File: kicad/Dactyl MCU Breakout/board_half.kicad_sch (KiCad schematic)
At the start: 30 parts, among them J301 JST, J302 Split, J303 Column, J304 Thumb, J305 External, J306 Row, J307 Display, J308 Vic, SW301 Battery, SW302 Reset, SW303 LED, U301 SRV05-4, U302 Nice!Nano/2040

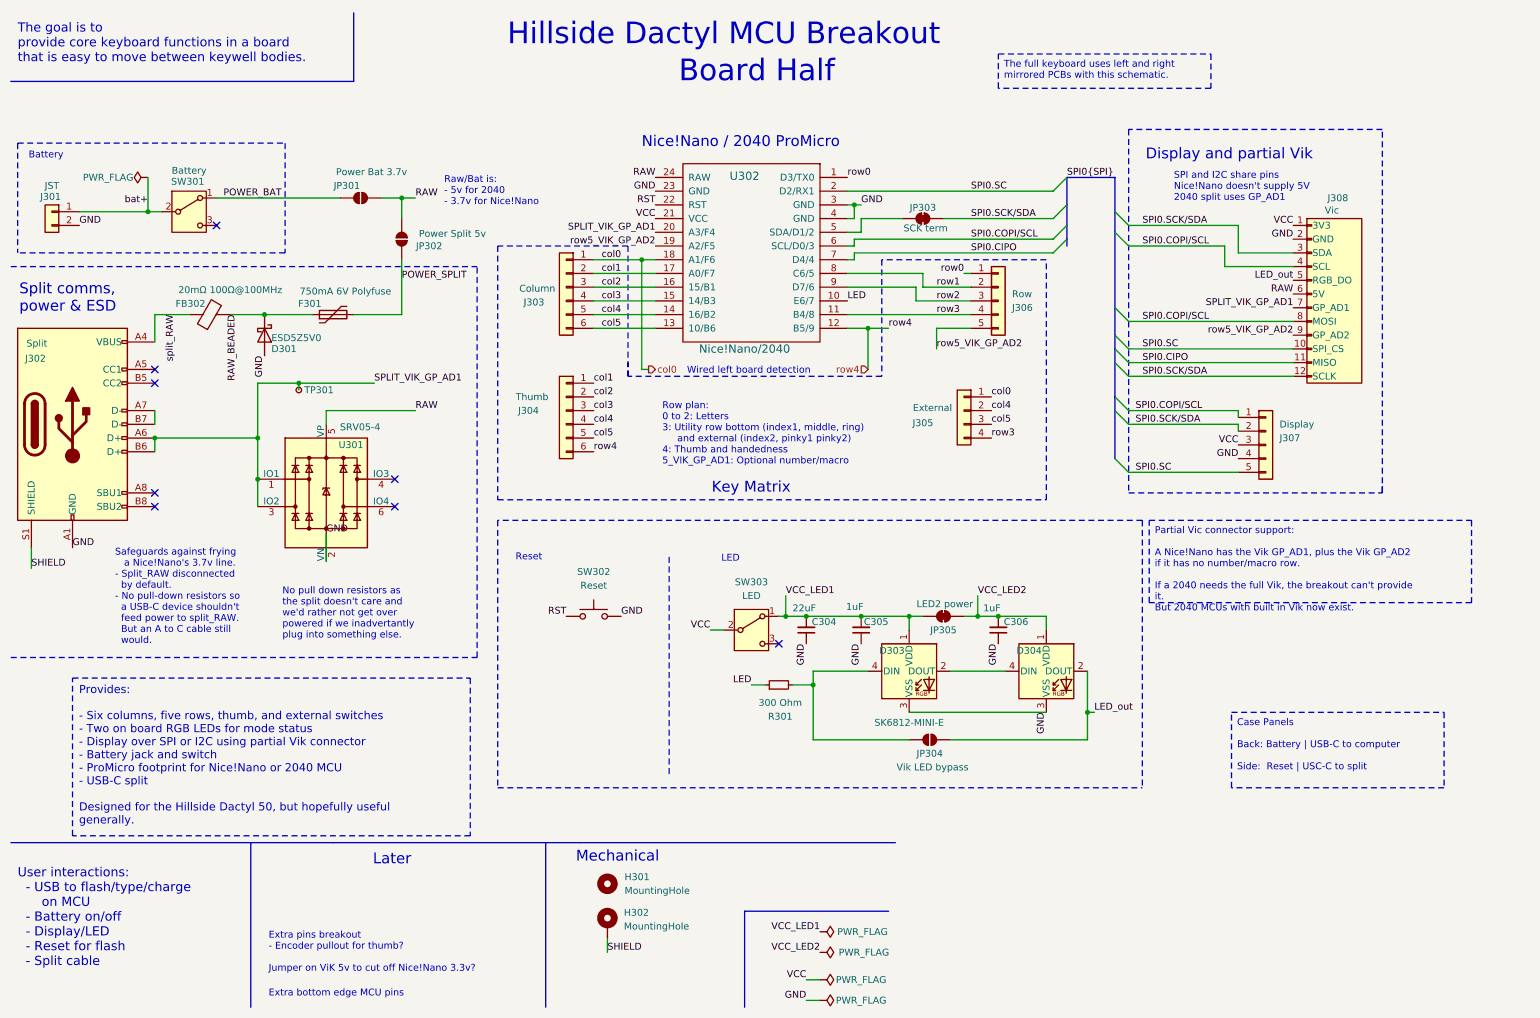
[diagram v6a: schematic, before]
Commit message: feat: split two wire crossed TX/RX UART
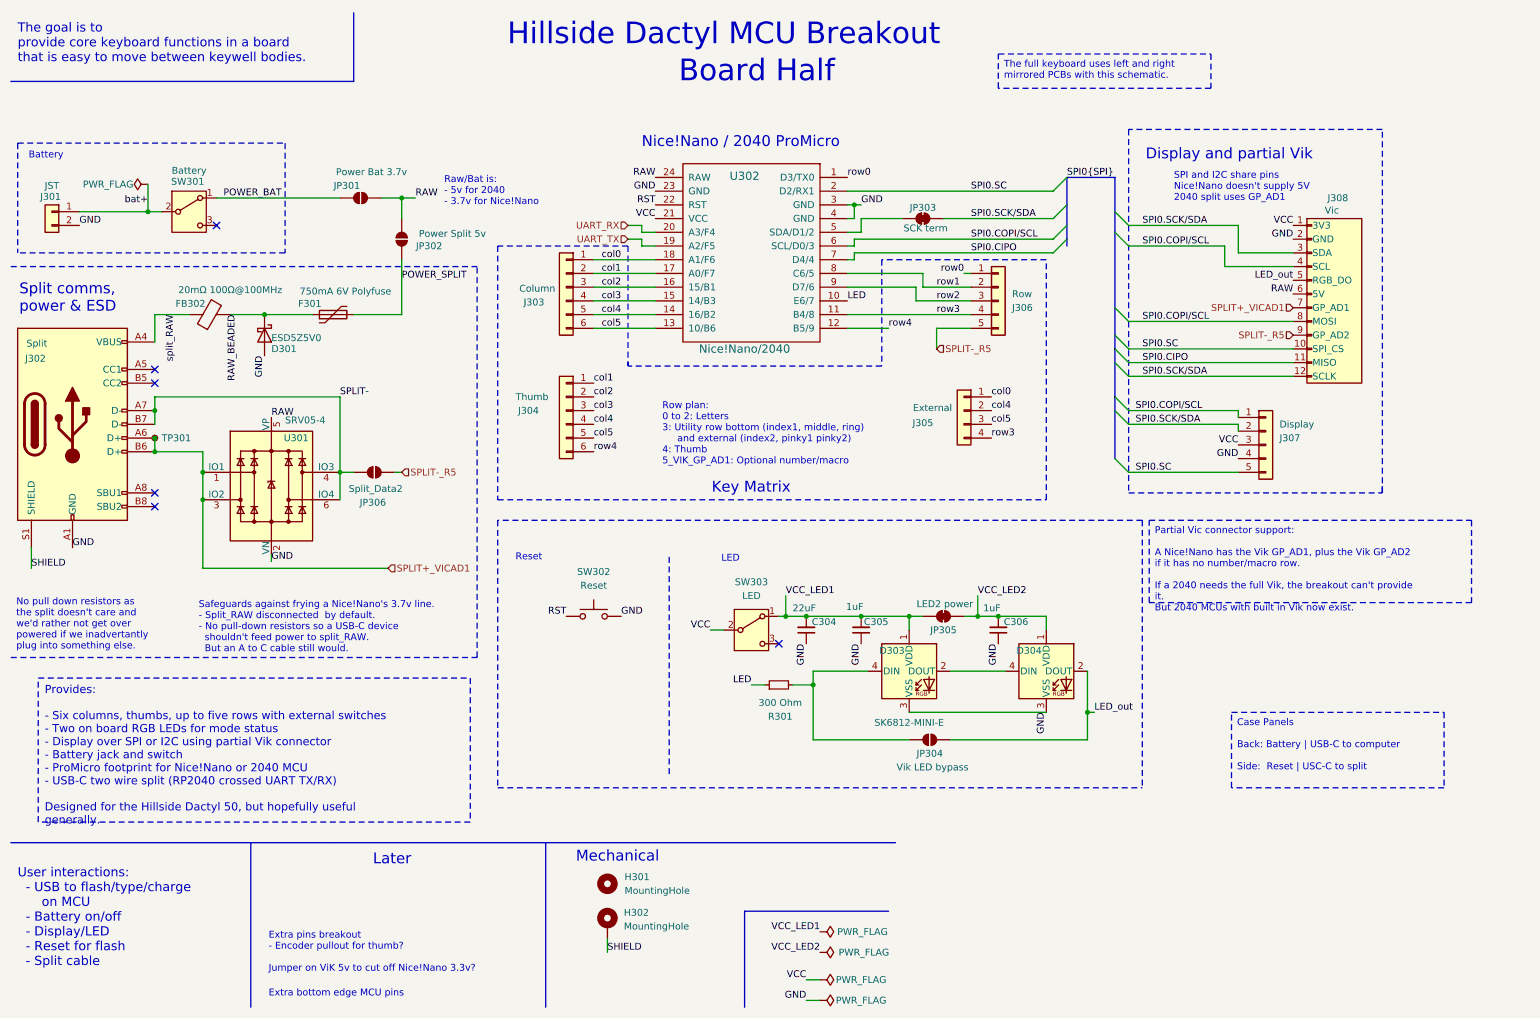
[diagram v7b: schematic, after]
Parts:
- added JP306: Split_Data2, Dactyl_basics:SolderJumper-2_P1.3mm_Open_RoundedPad1.0x1.5mm, symbol Jumper:SolderJumper_2_Open
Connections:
- net SPLIT-: now reaches U301.4 (IO3)
- net SPLIT-: now also J302.A7 (D-), J302.B7 (D-), U301.6 (IO4), JP306.1 (A)
- net SPLIT_VIK_GP_AD1 renamed SPLIT+_VICAD1
- net SPLIT+_VICAD1: no longer U302.20 (A3/F4)
- net row5_VIK_GP_AD2 renamed SPLIT-_R5
- net SPLIT-_R5: now also JP306.2 (B); no longer U302.19 (A2/F5)
- new net UART_RX: U302.20 (A3/F4)
- new net UART_TX: U302.19 (A2/F5)
- no-connect marks 8 -> 6
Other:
- note added: "Row plan: 0 to 2: Letters 3: Utility row bottom (index1, middle, ring) and external (index2, pinky1 pinky2) 4: Thumb 5_VIK_GP_AD1: Optional number/macro"
- note removed: "Row plan: 0 to 2: Letters 3: Utility row bottom (index1, middle, ring) and external (index2, pinky1 pinky2) 4: Thumb and handedness 5_VIK_GP_AD1: Optional number/macro"
- note removed: "Wired left board detection"
- moved on the sheet: U301
